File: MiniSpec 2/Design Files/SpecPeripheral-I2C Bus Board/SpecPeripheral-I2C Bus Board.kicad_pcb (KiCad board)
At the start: 2 copper layers, 65 x 95 mm, 8 parts, among them IC1 TCA9548APWR, J1 SSM-104-F-DV, J2 SSM-104-F-DV, J3 SSM-104-F-DV, J4 SSM-104-F-DV, J5 M20-7910442R

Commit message: Finished I2C Bus Board!
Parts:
- moved C1 1.10 mm to (147.9, 114.0)
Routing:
- net VCC: track 89.9 -> 92.3 mm
- added copper zone on F.Cu, net GND
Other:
- outline, holes or cut-outs redrawn

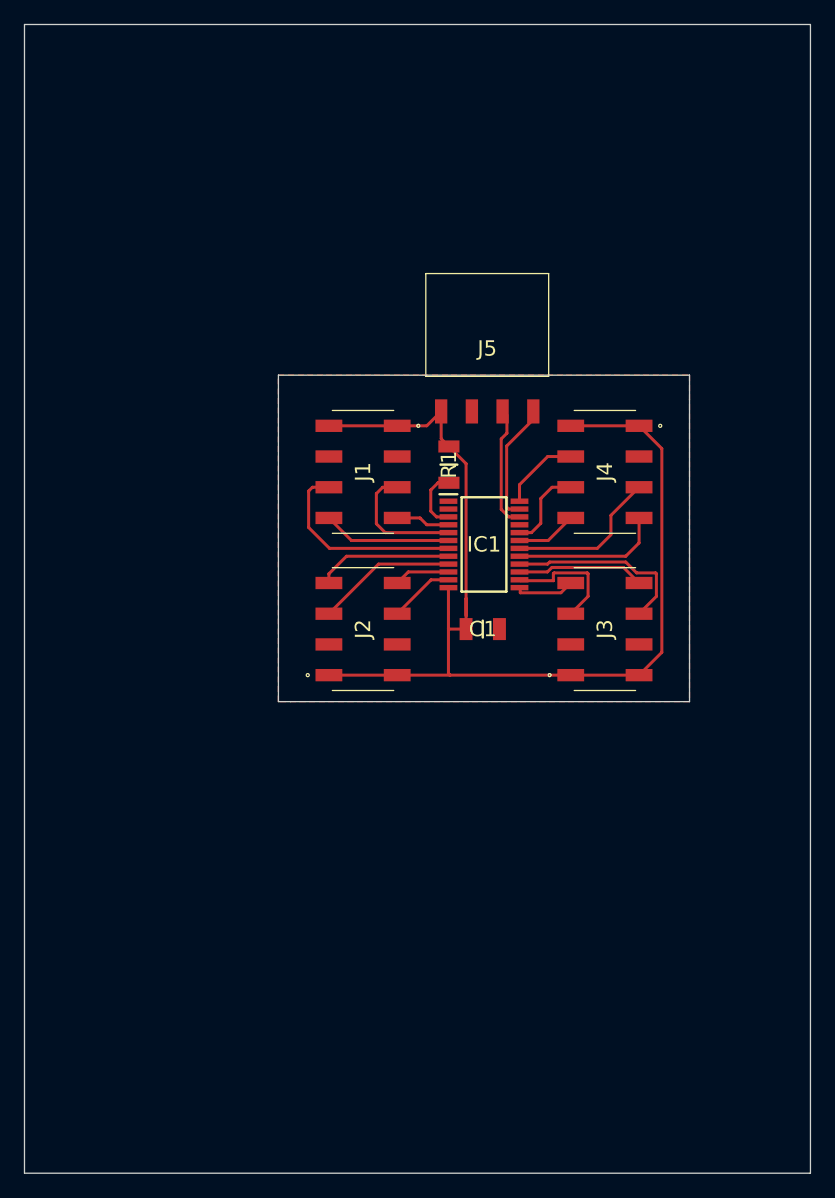
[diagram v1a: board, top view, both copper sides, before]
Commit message: Finished I2C Bus Board, added raw data of spec readings
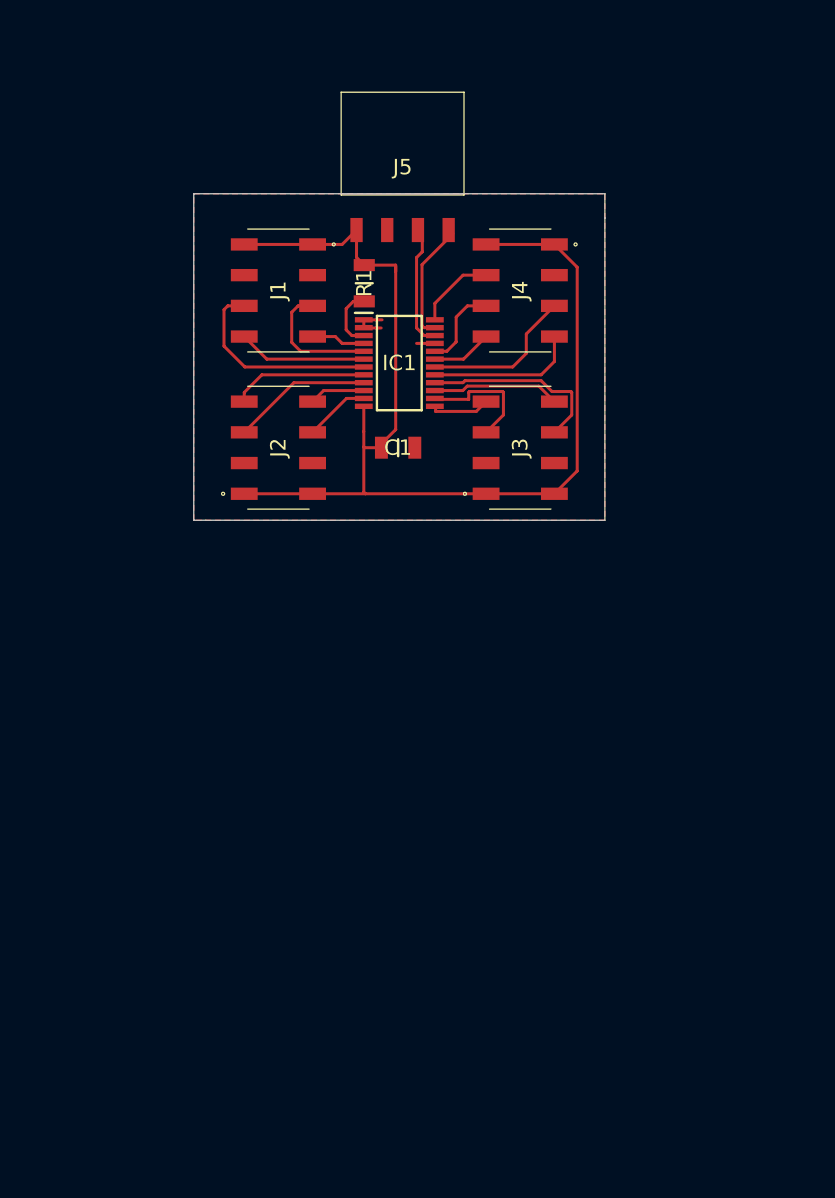
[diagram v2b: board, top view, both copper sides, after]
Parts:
- moved C1 16.6 mm to (140.9, 99.0)
- moved IC1 16.6 mm to (141.0, 92.0)
- moved J1 16.6 mm to (131.0, 86.0)
- moved J2 16.6 mm to (131.0, 99.0)
- moved J3 16.6 mm to (151.0, 99.0)
- moved J4 16.6 mm to (151.0, 86.0)
- moved J5 16.6 mm to (141.3, 75.8)
- moved R1 16.6 mm to (138.1, 85.4)
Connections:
- IC1 pad 1: (no net) -> GND
- IC1 pad 2: (no net) -> GND
- IC1 pad 21: (no net) -> GND
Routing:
- net GND: track 6.57 -> 11.7 mm
- net VCC: track 92.3 -> 93.8 mm
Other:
- board size 65 x 95 mm -> 34 x 27 mm

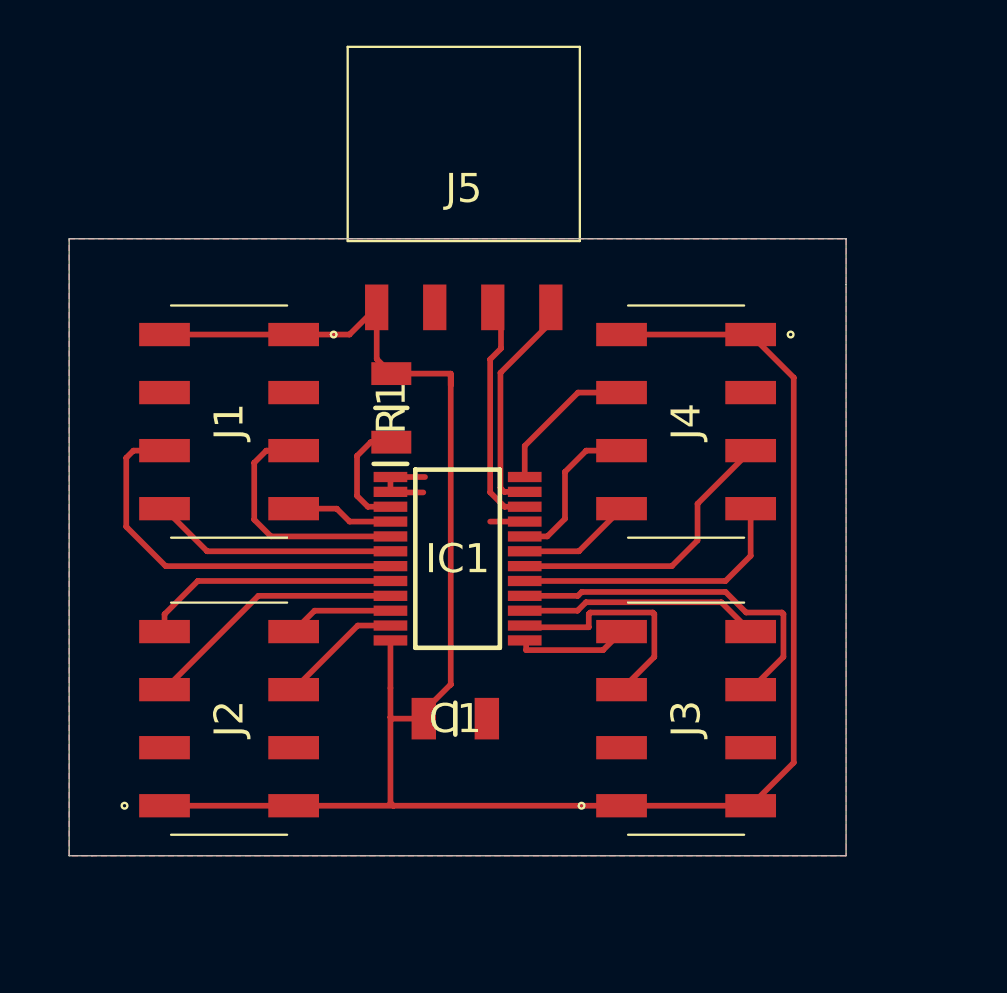
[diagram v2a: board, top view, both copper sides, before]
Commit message: respun I2C board with thicker traces for easier hand-etching
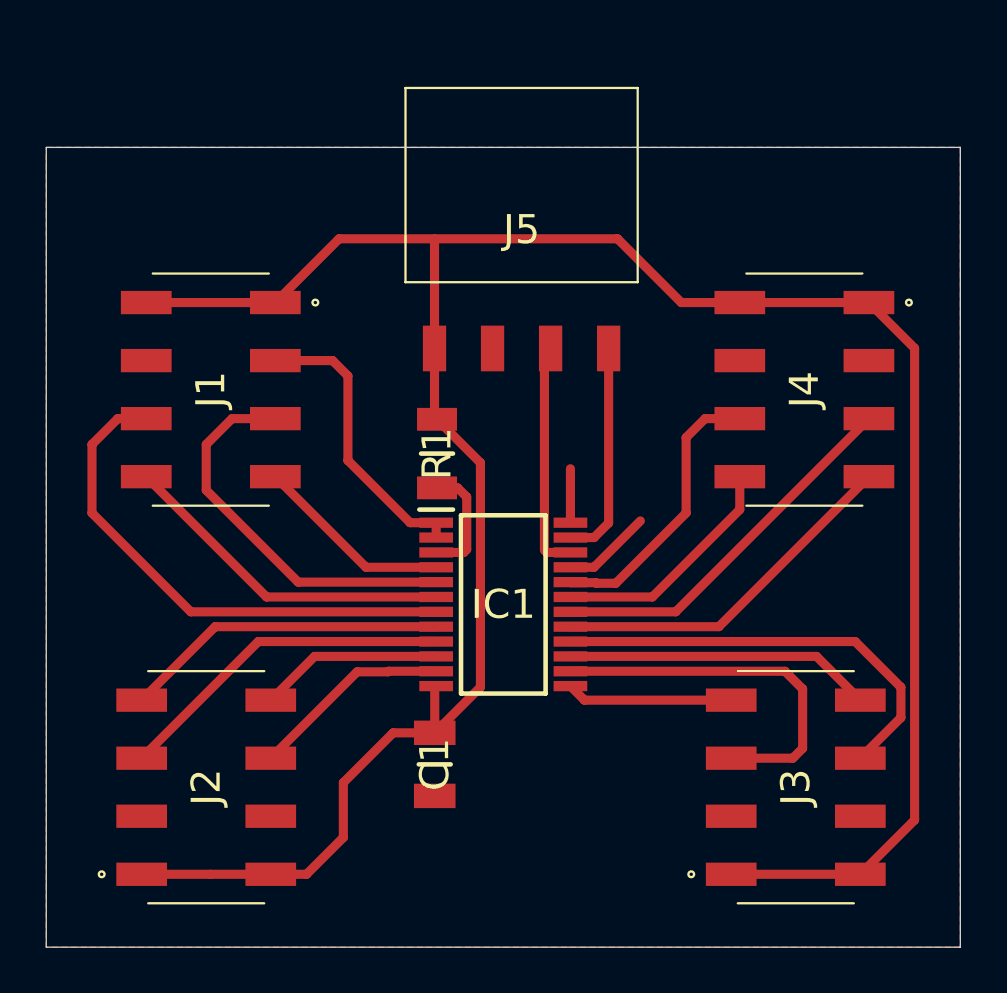
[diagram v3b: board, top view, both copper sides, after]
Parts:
- moved J3 5.66 mm to (155.8, 102.0)
- moved J4 5.36 mm to (156.2, 84.6)
- moved J2 3.16 mm to (130.0, 102.0)
- moved J5 3.10 mm to (143.8, 77.6)
- moved IC1 2.83 mm to (143.0, 94.0)
- moved R1 2.83 mm to (140.1, 87.4)
- moved C1 2.19 mm to (140.0, 101.0), turned to 270 degrees
- moved J1 1.61 mm to (130.2, 84.6)
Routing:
- net VCC: track 93.8 -> 108.6 mm
- net GND: track 11.7 -> 19.1 mm
- net SCL0: track 10.7 -> 17.2 mm
- net SCL4: track 10.2 -> 16.5 mm
- net SCL1: track 17.1 -> 22.7 mm
- net SDA7: track 5.01 -> 10.4 mm
- net SCL7: track 6.99 -> 12.4 mm
- net SDA1: track 10.7 -> 14.9 mm
- net SDA0: track 4.47 -> 8.68 mm
- net SCL6: track 12.9 -> 16.6 mm
- net SCL5: track 15.7 -> 19.1 mm
- net SCL2: track 11.6 -> 15.0 mm
- net SDA3: track 4.62 -> 8.03 mm
- net SCL3: track 5.40 -> 8.81 mm
- net SDA6: track 12.4 -> 15.8 mm
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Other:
- board size 34 x 27 mm -> 40 x 35 mm

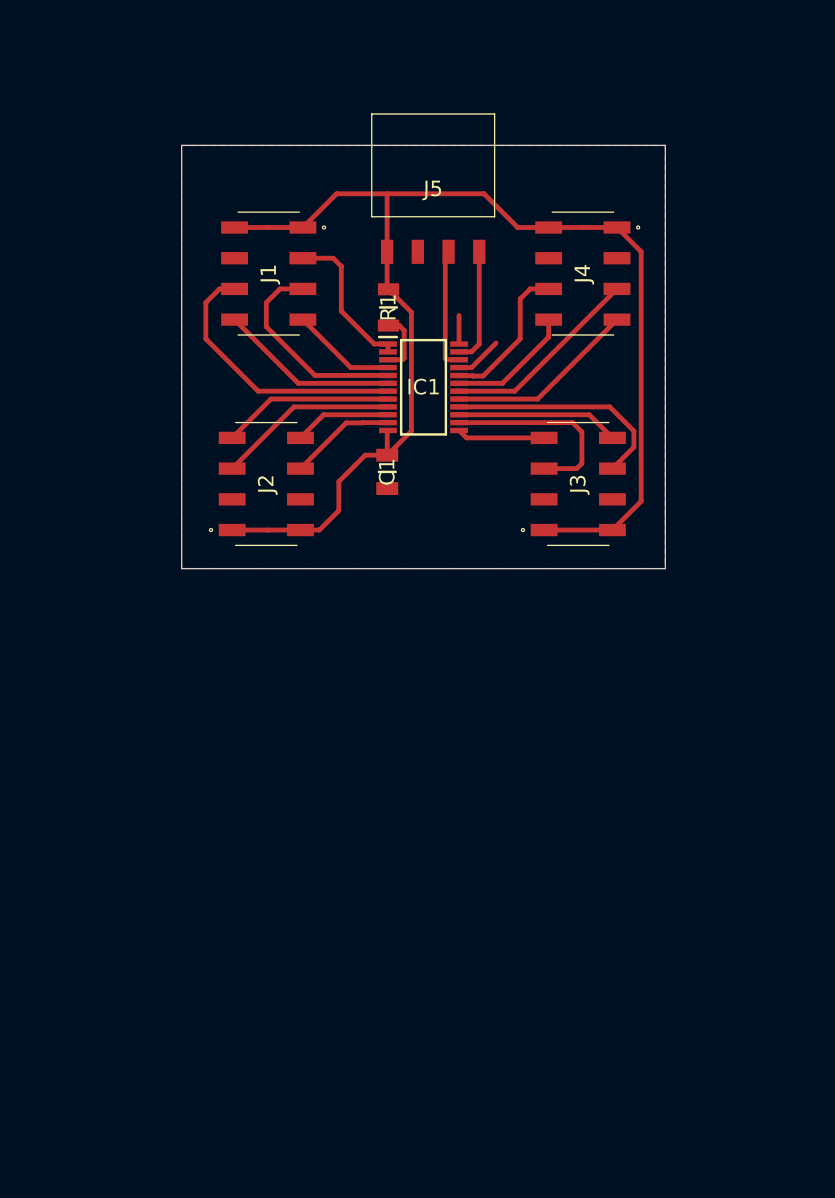
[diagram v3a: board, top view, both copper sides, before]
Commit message: big updates for 2 layer design with vias
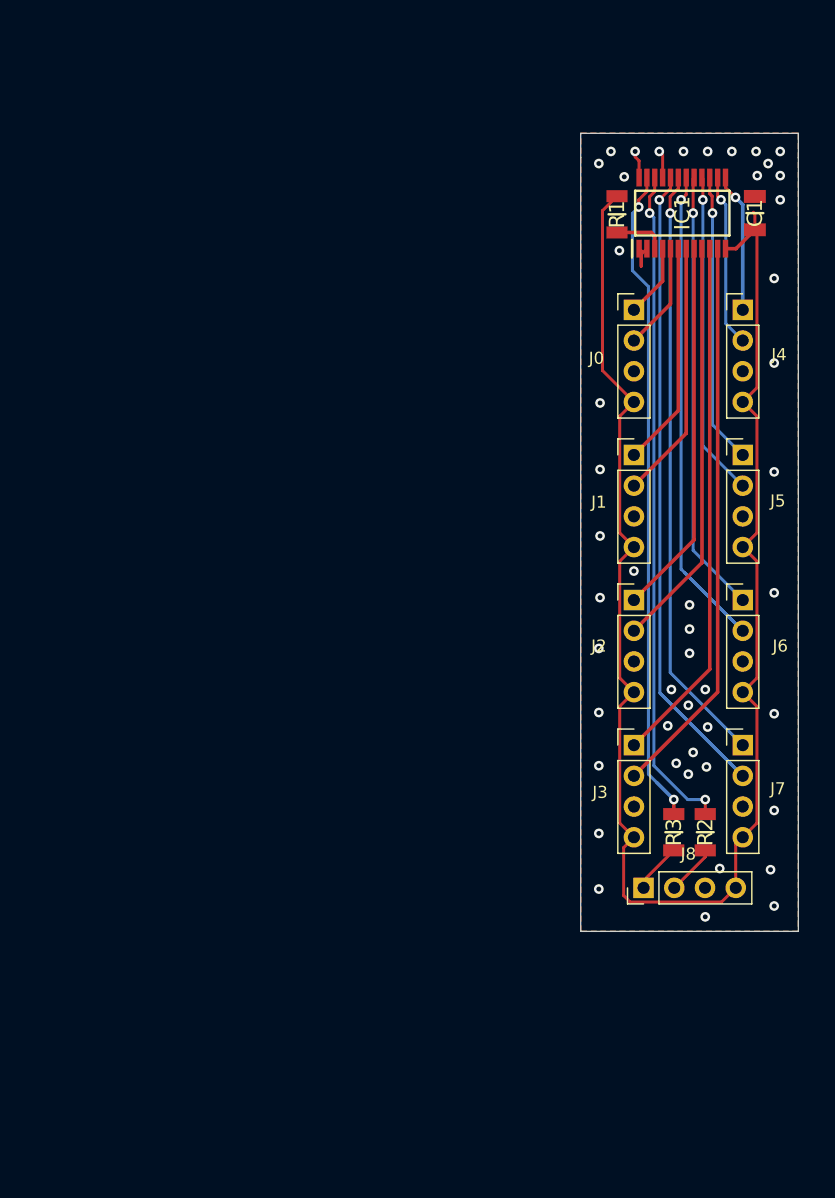
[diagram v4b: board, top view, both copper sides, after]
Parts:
- added J0: Conn_01x04_Female, Connector_PinHeader_2.54mm:PinHeader_1x04_P2.54mm_Vertical, F.Cu at (160.4, 87.6)
- added J6: Conn_01x04_Female, Connector_PinHeader_2.54mm:PinHeader_1x04_P2.54mm_Vertical, F.Cu at (169.4, 111.6)
- added J7: Conn_01x04_Female, Connector_PinHeader_2.54mm:PinHeader_1x04_P2.54mm_Vertical, F.Cu at (169.4, 123.6)
- added J8: Conn_01x04_Female, Connector_PinHeader_2.54mm:PinHeader_1x04_P2.54mm_Vertical, F.Cu at (161.2, 135.4)
- added R2: 10K, SamacSys_Parts:RESC3116X65N, F.Cu at (166.3, 130.8)
- added R3: 10K, SamacSys_Parts:RESC3116X65N, F.Cu at (163.7, 130.8)
- J1, J2, J3, J4: value SSM-104-F-DV -> Conn_01x04_Female; footprint SamacSys_Parts:SSM-104-XXX-DV -> Connector_PinHeader_2.54mm:PinHeader_1x04_P2.54mm_Vertical
- J5: value M20-7910442R -> Conn_01x04_Female; footprint SamacSys_Parts:M207910442R -> Connector_PinHeader_2.54mm:PinHeader_1x04_P2.54mm_Vertical
- moved C1 37.2 mm to (170.4, 79.6), turned to 90 degrees
- moved J5 33.8 mm to (169.4, 99.6)
- moved J1 33.7 mm to (160.4, 99.6), turned to 0 degrees
- moved J2 31.9 mm to (160.4, 111.6), turned to 0 degrees
- moved IC1 25.8 mm to (164.4, 79.6), turned to 90 degrees
- moved J3 22.1 mm to (160.4, 123.6), turned to 0 degrees
- moved R1 20.4 mm to (159.0, 79.7)
- moved J4 13.6 mm to (169.4, 87.6), turned to 0 degrees
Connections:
- J1 pad 1: VCC -> SDA1
- J1 pad 2: VCC -> SCL1
- J1 pad 4: GND -> VCC
- J2 pad 1: VCC -> SDA2
- J2 pad 2: VCC -> SCL2
- J2 pad 4: GND -> VCC
- J3 pad 1: VCC -> SDA3
- J3 pad 2: VCC -> SCL3
- J3 pad 4: GND -> VCC
- J4 pad 1: VCC -> SDA4
- J4 pad 2: VCC -> SCL4
- J4 pad 4: GND -> VCC
- J5 pad 1: VCC -> SDA5
- J5 pad 2: GND -> SCL5
- J5 pad 3: SCLMC -> GND
- J5 pad 4: SDAMC -> VCC
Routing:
- net SCL7: track 12.4 -> 62.3 mm, vias 0 -> 1
- net SCLMC: track 10.1 -> 55.6 mm, vias 0 -> 2
- net SDAMC: track 9.57 -> 54.6 mm, vias 0 -> 2
- net SDA7: track 10.4 -> 49.7 mm, vias 0 -> 1
- net SCL3: track 8.81 -> 46.5 mm
- net SDA3: track 8.03 -> 43.7 mm
- net SCL6: track 16.6 -> 46.6 mm, vias 0 -> 1
- net VCC: track 108.6 -> 136.0 mm
- net SDA6: track 15.8 -> 36.7 mm, vias 0 -> 1
- net SCL2: track 15.0 -> 33.9 mm
- net SDA2: track 14.2 -> 31.1 mm
- net GND: track 19.1 -> 7.77 mm, vias 0 -> 46
- net SDA5: track 13.5 -> 24.1 mm, vias 0 -> 1
- net SCL0: track 17.2 -> 8.85 mm
- net SCL5: track 19.1 -> 27.0 mm, vias 0 -> 1
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- added copper zone on B.Cu, net GND
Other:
- board size 40 x 35 mm -> 18 x 66 mm

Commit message: added latest TSL2572 curves in Raw Data folder
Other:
- net class Default removed
